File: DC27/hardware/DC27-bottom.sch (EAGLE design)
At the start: 2 parts

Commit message: removed inputs to output pins....duh
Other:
- note added: "Put a jumper between the FT2232HL and the rx/tx of the ESP. This will allow for using a usb to serial that isn't the FT2232HL otherwise the FT2232HL keeps the pins high"
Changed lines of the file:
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@@
 <drawing>
 <settings>
-<setting alwaysvectorfont="no"/>
+<setting alwaysvectorfont="yes"/>
 <setting verticaltext="up"/>
 </settings>
@@
 </instances>
 <busses>
+</busses>
+<nets>
+</nets>
+</sheet>
+<sheet>
+<plain>
+<text x="-10.16" y="81.28" size="1.778" layer="91">Put a jumper between the FT2232HL and the rx/tx of the ESP. This will allow for using a usb to serial that isn't the FT2232HL otherwise the FT2232HL keeps the pins high</text>
+</plain>
+<instances>
+</instances>
+<busses>

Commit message: moving over schema
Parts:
- removed U$2: CMD_C0DE_LOGO, darknet_parts_library:CMD_C0DE_LOGO
- added ATTINY13A: Header, connector:M06SILK_FEMALE_PTH
- added C1, C13, C22, C23, C24, C25: 10 uf, passives:C-USC0805
- added C10, C11, C12, C14, C15, C16, C17, C19, C21, C3, C32, C35, C8: 0.1 uF, passives:C-USC0805
- added C18, C2, C20: 4.7 uF, passives:C-USC0805
- added C26, C27, C28, C29: 15 pF, passives:C-USC0805
- added C33, C34: 10 uF, passives:C-USC0805
- added C4, C5: 1 uF, passives:C-USC0805
- added C6, C7: 27 pF, passives:C-USC0805
- added C9: 3.3 uF, passives:C-USC0805
- added D1: (no value), passives:DIODESMA
- added EMIFILTER1, EMIFILTER2: MEM2012S101RT, passives:MEM2012S101RT
- added ESP-PROG, ESP-RST: UserButton, dc-26:SWITCH_TACTILETACTILE-2PIN-NARROW
- added F1: ABLS-12.000MHZ-B4-T, crystals-timing:ABLS-12.000MHZ-B4-T
- added IC-IP5305: IP5305ESOP8, charging-ic:IP5305ESOP8
- added IC1: ATTINY13A-SSU, ICs:ATTINY13A-SSU
- added IC2: LDL112D33R, voltage-regulator:LDL112D33R
- added IC3: FT2232HL-REEL, ICs:FT2232HL-REEL
- added IC4: 93LC46BT-I_OT, eeprom:93LC46BT-I_OT
- added IC5, IC6, IC7, IC8: APA104, leds:APA104
- added J1: (no value), connector:M14
- added J3: (no value), connector:M02JST-PTH-2
- added J4: DN PAIR, connector:M04PTH
- added J8: (no value), connector:M06NO_SILK_YES_STOP
- added L1: 2.2uH, passives:NRS4018T2R2MDGJ
- added LED1, LED4, LED5, LED6, LED7, LED8: (no value), leds:LED3MM
- added LED2: rx-led, leds:LED3MM
- added LED3: tx-led, leds:LED3MM
- added OFF/ON: (no value), switches:SWITCH-SPSTPTH
- added R1, R4: 10K, dc-26:RESISTOR0805-RES
- added R10: 2.2K, passives:RESISTOR0805-RES
- added R11, R12: 56, passives:RESISTOR0805-RES
- added R13, R14: 100 R, passives:RESISTOR0805-RES
- added R15, R18, R19, R20: 100 R, dc-26:RESISTOR0805-RES
- added R16: 4.7 K, passives:RESISTOR0805-RES
- added R17, R22: 10 K, passives:RESISTOR0805-RES
- added R2: 10 R, passives:RESISTOR0805-RES
- added R21: 4K7, passives:RESISTOR0805-RES
- added R3: 20 R, passives:RESISTOR0805-RES
- added R5: 1K, passives:RESISTOR0805-RES
- added R6: 12 K, passives:RESISTOR0805-RES
- added R7, R8, R9: 10K, passives:RESISTOR0805-RES
- added RESETTABLE_FUSE: 0ZCJ0050FF2G, passives:0ZCJ0050FF2G
- added U$3: DX4R005JJ2DX4R005JJ2, connector:DX4R005JJ2DX4R005JJ2
- added U$4: ATECC608A-SSHDA, ICs:ATECC608A-SSHDA
- added U$5: SWITCH_TACTILETACTILE-2PIN-NARROW, switches:SWITCH_TACTILETACTILE-2PIN-NARROW
- added U$6: DC-27-SAO, defcon:DC-27-SAO
- added U$7: KRUX_LOGO, logos:KRUX_LOGO
- added U$8: CMD_C0DE_LOGO, logos:CMD_C0DE_LOGO
- added U$9: DN_LOGODC26, logos:DN_LOGODC26
- added U2: ESP-WROOM-32, ICs:ESP-WROOM-32
- U$1: value KRUX_LOGO -> M06X2; device darknet_parts_library:KRUX_LOGO -> connector:M06X2
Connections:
- new net ATTINY_ESP_CON: ATTINY13A.2, IC1.[PCINT3/CLKI/ADC3]_PB3, R19.1
- new net DISPLAY_BACKLIT: C34.1, J1.4, R18.2
- new net DISPLAY_CS: J1.5, U2.IO17
- new net DISPLAY_DATA_CMD: J1.3, U2.IO4
- new net DISPLAY_RESET: C2.1, J1.2, R15.2
- new net DISPLAY_SD_MISO: J1.8, U2.IO19
- new net DISPLAY_SD_MOSI: J1.13, U2.IO23
- new net DISPLAY_SD_SCK: J1.7, U2.IO18
- new net EECLK: IC3.EECLK, IC4.CLK, R8.2
- new net EECS: IC3.EECS, IC4.CS, R7.1
- new net EEDATA: IC3.EEDATA, IC4.DI, R10.2
- new net ESP-EN: ESP-RST.C, R4.1, U2.EN
- new net ESP-IO0: ESP-PROG.A, R1.1, U2.IO0
- new net ESP_ATTINY_CON: R19.2, U2.IO2
- new net ESP_LED1: R20.2, U2.IO16
- new net GND: C1.2, C10.2, C11.2, C12.2, C13.1, C14.2, C15.2, C16.2, C17.2, C18.2, C19.2, C2.2, C20.2, C21.2, C22.1, C23.1, C24.1, C25.2, C26.2, C27.2, C28.2, C29.2, C3.2, C32.2, C33.2, C34.2, C35.2, C4.2, C5.2, C6.2, C7.2, C8.2, C9.2, EMIFILTER1.GND_1, EMIFILTER1.GND_2, EMIFILTER2.GND_1, EMIFILTER2.GND_2, ESP-PROG.C, ESP-RST.A, IC-IP5305.9, IC1.GND, IC2.GND(1), IC2.GND(2), IC2.GND(3), IC2.GND(4), IC3.AGND, IC3.GND_1, IC3.GND_2, IC3.GND_3, IC3.GND_4, IC3.GND_5, IC3.GND_6, IC3.GND_7, IC3.GND_8, IC3.TEST, IC4.VSS, IC5.VSS, IC6.VSS, IC7.VSS, IC8.VSS, J1.14, J3.2, J8.3, LED7.C, LED8.C, OFF/ON.O, R22.1, R6.2, U$1.2, U$3.GND, U$4.GND, U$5.A, U$6.GND, U2.GND, U2.GND@1, U2.GND@15, U2.GND@38
- new net GPIO_APA104_DATA: ATTINY13A.1, IC1.[PCINT4/ADC2]_PB4, IC5.DIN
- new net JTAG_CLK: IC3.ADBUS0, U2.IO13
- new net JTAG_TDI: IC3.ADBUS1, U2.IO12
- new net JTAG_TDO: IC3.ADBUS2, U2.IO15
- new net JTAG_TMS: IC3.ADBUS3, U2.IO14
- new net N$1: D1.C, U$6.3V3
- new net N$10: C23.2, C24.2, IC-IP5305.8, RESETTABLE_FUSE.1
- new net N$11: LED2.A, R11.1
- new net N$12: IC6.DOUT, IC7.DIN
- new net N$13: LED3.A, R12.1
- new net N$14: IC-IP5305.3, LED5.A, LED6.C
- new net N$15: IC-IP5305.4, LED1.C, LED4.A, LED5.C, LED6.A
- new net N$16: C22.2, R2.2
- new net N$17: IC-IP5305.7, L1.2
- new net N$18: C18.1, C19.1, EMIFILTER2.OUT/IN, IC3.VPLL
- new net N$19: C20.1, C21.1, EMIFILTER1.OUT/IN, IC3.VPHY
- new net N$2: IC2.EN, OFF/ON.P
- new net N$20: C25.1, IC-IP5305.6, J3.1, L1.1
- new net N$21: IC-IP5305.5, R17.1, R3.1
- new net N$22: IC7.DOUT, IC8.DIN
- new net N$24: LED7.A, R3.2
- new net N$25: R17.2, U$5.C
- new net N$31: R14.1, U$1.9
- new net N$32: R13.1, U$1.7
- new net N$4: IC5.DOUT, IC6.DIN
- new net N$5: IC-IP5305.2, LED1.A, LED4.C
- new net N$6: IC3.RESET#, R5.2
- new net N$7: IC3.REF, R6.1
- new net N$8: IC4.DO, R10.1, R9.1
- new net N$9: LED8.A, R20.1
- new net OSCI: C6.1, F1.A, IC3.OSCI
- new net OSCO: C7.1, F1.K, IC3.OSCO
- new net PAIR_RX: J4.2, U2.IO34
- new net PAIR_TX: J4.1, U2.IO25
- new net PB0: ATTINY13A.6, IC1.PB0_[MOSI/AIN0/OC0A/PCINT0]
- new net PB1: ATTINY13A.5, IC1.PB1_[MISO/AIN1/OC0B/INT0/PCINT1]
- new net PB2: ATTINY13A.4, IC1.PB2_[SCK/ADC1/T0/PCINT2]
- new net PB5: ATTINY13A.3, IC1.PCINT5/!RESET!/ADC0/DW]_PB5, R16.1
- new net PROG_RX: R14.2, U2.RXD0
- new net PROG_TX: R13.2, U2.TXD0
- new net PWREN: IC3.PWREN#, U$1.1
- new net PWRSAV: IC3.BCBUS7, R21.2, R22.2
- new net RXD_LED: IC3.BCBUS3, LED2.C
- new net RXD_SPI_PROM_MOSI: IC3.BDBUS1, J1.11, U$1.8
- new net SAO-GPIO1: U$6.GPIO1
- new net SAO-GPIO2: U$6.GPIO2
- new net SCL: J1.12, U$4.SCL, U$6.SCL, U2.IO22
- new net SDA: J1.9, U$4.SDA, U$6.SDA, U2.IO21
- new net SD_CS: J1.6, U2.IO5
- new net SPI_PROM_CS: IC3.BDBUS3, U$1.4
- new net SPI_PROM_MISO: IC3.BDBUS2, U$1.6
- new net SUSPEND: IC3.SUSPEND__#, U$1.3
- new net SVN: J4.3, U2.SENSOR_VN
- new net SVP: J4.4, U2.SENSOR_VP
- new net TOUCH_CLK: J8.2, U2.IO26
- new net TOUCH_CS: J8.1, U2.IO27
- new net TOUCH_DATA_IN: J8.6, U2.IO35
- new net TOUCH_DATA_OUT: J8.4, U2.IO33
- new net TOUCH_IRQ: J8.5, U2.IO32
- new net TXD_LED: IC3.BCBUS4, LED3.C
- new net TXD_SPI_PROM_CLK: IC3.BDBUS0, J1.10, U$1.10
- new net USB_DM: IC3.DM, U$3.D-
- new net USB_DP: IC3.DP, U$3.D+
- new net VBAT: C26.1, C27.1, C28.1, C29.1, C32.1, C33.1, C4.1, IC1.VCC, IC2.VIN, IC5.VDD, IC6.VDD, IC7.VDD, IC8.VDD, OFF/ON.S, R16.2, RESETTABLE_FUSE.2
- new net VCC: C1.1, C11.1, C14.1, C15.1, C16.1, C3.1, C35.1, C5.1, C8.1, D1.A, EMIFILTER1.IN/OUT, EMIFILTER2.IN/OUT, IC2.VOUT, IC3.VCCIO_1, IC3.VCCIO_2, IC3.VCCIO_3, IC3.VCCIO_4, IC3.VREGIN, IC4.VCC, J1.1, R1.2, R11.2, R12.2, R15.1, R18.1, R4.2, R5.1, R7.2, R8.1, R9.2, U$1.12, U$4.VCC, U2.3V3
- new net VCC1.8: C10.1, C12.1, C17.1, C9.1, IC3.VCORE_1, IC3.VCORE_2, IC3.VCORE_3, IC3.VREGOUT
- new net VCC5V: C13.2, IC-IP5305.1, R2.1, R21.1, U$3.+5V
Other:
- note added: "If we don't connect RESX line to a GPIO (and I'm not to save GPIO pins), we need to ensure RESX stay low for 10 us. So I'm going to set it up to stay low via a capacitor for 470 us by using a 4.7 uF cap and a 100 Ohm resistor calculator used: https://www.allaboutcircuits.com/tools/capacitor-Charge-and-time-constant-calculator/ same for back light, except using a larger cap to delay even longer"
- note added: "Pins 60, 36, and 59 need to be revisited to allow for external control of suspend."
- note added: "output pins: pwren: low = normal, high USB suspend suspend: low when in USB suspend"
- note added: "vcc5v is from USB. If usb plugged in pwrsav goes high and ft2232HL turns on, if unplugged it turns off."

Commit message: dc27 board started for darknet 8
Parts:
- removed ATTINY13A: Header, connector:M06SILK_FEMALE_PTH
- removed C32: 0.1 uF, passives:C-USC0805
- removed C33: 10 uF, passives:C-USC0805
- removed F1: ABLS-12.000MHZ-B4-T, crystals-timing:ABLS-12.000MHZ-B4-T
- removed IC1: ATTINY13A-SSU, ICs:ATTINY13A-SSU
- removed IC5, IC6, IC7, IC8: APA104, leds:APA104
- removed J4: DN PAIR, connector:M04PTH
- removed J8: (no value), connector:M06NO_SILK_YES_STOP
- removed R19, R20: 100 R, dc-26:RESISTOR0805-RES
- removed R21: 4K7, passives:RESISTOR0805-RES
- added J2: JTAG, connector:M04X2
- added R23, R24, R25, R26: 100 R, dc-26:RESISTOR0805-RES
- added U$10: 2.4-SPI-TFT-TOUCH-SSD-MODULE, displays:2.4-SPI-TFT-TOUCH-SSD-MODULE
- added U$11, U$12, U$13, U$14: APA1025050, leds:APA1025050
- added U$2: XBP15SRV05W-G, passives:XBP15SRV05W-G
- added Y1: ABM7-12.000MHZ-D2Y-T, crystals-timing:ABM7-12.000MHZ-D2Y-T
- C1, C13, C22, C23, C24, C25: value 10 uf -> 10 uF
- C6, C7: value 27 pF -> 18 pF
- D1: value (none) -> SAO-Diode
- J1: value (none) -> DN PAIR; device connector:M14 -> connector:M03X22X3_SILK_MALE_PTH
- J3: value (none) -> Battery
- LED1: value (none) -> cl1
- LED4: value (none) -> cl2
- LED5: value (none) -> cl3
- LED6: value (none) -> cl4
- LED7: value (none) -> KeyLed
- LED8: value (none) -> ESP-LED
- OFF/ON: value (none) -> Brd Power; device switches:SWITCH-SPSTPTH -> switches:SWITCH-SPSTKIT
- R1, R4, R7, R8, R9: value 10K -> 10 K
- R10: value 2.2K -> 2.2 K
- R11, R12: value 56 -> 56 R
- R3: value 20 R -> 10 R
- R5: value 1K -> 1 K
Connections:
- removed net ATTINY_ESP_CON: ATTINY13A.2, IC1.[PCINT3/CLKI/ADC3]_PB3, R19.1
- removed net ESP_ATTINY_CON: R19.2, U2.IO2
- removed net ESP_LED1: R20.2, U2.IO16
- removed net GPIO_APA104_DATA: ATTINY13A.1, IC1.[PCINT4/ADC2]_PB4, IC5.DIN
- removed net JTAG_TDO: IC3.ADBUS2, U2.IO15
- removed net N$12: IC6.DOUT, IC7.DIN
- removed net N$22: IC7.DOUT, IC8.DIN
- removed net N$4: IC5.DOUT, IC6.DIN
- removed net N$9: LED8.A, R20.1
- removed net PB0: ATTINY13A.6, IC1.PB0_[MOSI/AIN0/OC0A/PCINT0]
- removed net PB1: ATTINY13A.5, IC1.PB1_[MISO/AIN1/OC0B/INT0/PCINT1]
- removed net PB2: ATTINY13A.4, IC1.PB2_[SCK/ADC1/T0/PCINT2]
- removed net PB5: ATTINY13A.3, IC1.PCINT5/!RESET!/ADC0/DW]_PB5, R16.1
- new net APA102_CLK: U$13.CI, U2.IO2
- new net APA102_DATA: U$13.DI, U2.IO16
- new net ESP_JTAG_CLK: J2.8, R23.1
- new net ESP_JTAG_TDI: J2.6, R25.1
- new net ESP_JTAG_TDO_LED: J2.4, LED8.A, R24.1
- new net ESP_JTAG_TMS: J2.2, R26.1
- new net FT_JTAG_CLK: IC3.ADBUS0, J2.7
- new net FT_JTAG_TDI: IC3.ADBUS1, J2.5
- new net FT_JTAG_TDO: IC3.ADBUS2, J2.3
- new net FT_JTAG_TMS: IC3.ADBUS3, J2.1
- new net JTAG_TDO_LED1: R24.2, U2.IO15
- new net N$28: U$11.GND, U$12.GND, U$13.GND, U$14.GND
- new net N$34: U$11.CI, U$12.CO
- new net N$35: U$11.DI, U$12.DO
- new net N$36: U$12.CI, U$14.CO
- new net N$37: U$12.DI, U$14.DO
- new net N$38: U$13.DO, U$14.DI
- new net N$39: U$13.CO, U$14.CI
- net DISPLAY_BACKLIT: now also U$10.LED; no longer J1.4
- net DISPLAY_CS: now also U$10.CS; no longer J1.5
- net DISPLAY_DATA_CMD: now also U$10.D/C; no longer J1.3
- net DISPLAY_RESET: now also U$10.RESET; no longer J1.2
- net DISPLAY_SD_MISO: now also U$10.MISO, U$10.SD_MISO; no longer J1.8
- net DISPLAY_SD_MOSI: now also U$10.MOSI, U$10.SD_MOSI; no longer J1.13
- net DISPLAY_SD_SCK: now also U$10.SCK, U$10.SD_SCK; no longer J1.7
- net ESP-IO0: now also ESP-PROG.C; no longer ESP-PROG.A
- net GND: now also ESP-PROG.A, U$10.GND, U$2.P2; no longer C32.2, C33.2, ESP-PROG.C, IC1.GND, IC5.VSS, IC6.VSS, IC7.VSS, IC8.VSS, J1.14, J8.3
- net JTAG_CLK: now also R23.2; no longer IC3.ADBUS0
- net JTAG_TDI: now also R25.2; no longer IC3.ADBUS1
- net JTAG_TMS: now also R26.2; no longer IC3.ADBUS3
- net OSCI: now also Y1.2; no longer F1.A
- net OSCO: now also Y1.1; no longer F1.K
- net PAIR_RX: now also J1.3; no longer J4.2
- net PAIR_TX: now also J1.5; no longer J4.1
- net PWRSAV: now also R16.2; no longer R21.2
- net RXD_SPI_PROM_MOSI: no longer J1.11
- net SAO-GPIO1: now also J1.4
- net SAO-GPIO2: now also J1.6
- net SCL: no longer J1.12
- net SDA: no longer J1.9
- net SD_CS: now also U$10.SD_CS; no longer J1.6
- net SVN: now also J1.1; no longer J4.3
- net SVP: now also J1.2; no longer J4.4
- net TOUCH_CLK: now also U$10.T_CLK; no longer J8.2
- net TOUCH_CS: now also U$10.T_CS; no longer J8.1
- net TOUCH_DATA_IN: now also U$10.T_DIN; no longer J8.6
- net TOUCH_DATA_OUT: now also U$10.T_DO; no longer J8.4
- net TOUCH_IRQ: now also U$10.T_IRQ; no longer J8.5
- net TXD_SPI_PROM_CLK: no longer J1.10
- net USB_DM: now also U$2.P1
- net USB_DP: now also U$2.P6
- net VBAT: no longer C26.1, C27.1, C28.1, C29.1, C32.1, C33.1, IC1.VCC, IC5.VDD, IC6.VDD, IC7.VDD, IC8.VDD, R16.2
- net VCC: now also C26.1, C27.1, C28.1, C29.1, U$10.VCC, U$11.VCC, U$12.VCC, U$13.VCC, U$14.VCC; no longer J1.1
- net VCC5V: now also R16.1; no longer R21.1
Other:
- note added: "dn pair: can jumper pair pins to sao gpio pins"
- note removed: "Pins 60, 36, and 59 need to be revisited to allow for external control of suspend."
- note removed: "Put a jumper between the FT2232HL and the rx/tx of the ESP. This will allow for using a usb to serial that isn't the FT2232HL otherwise the FT2232HL keeps the pins high"

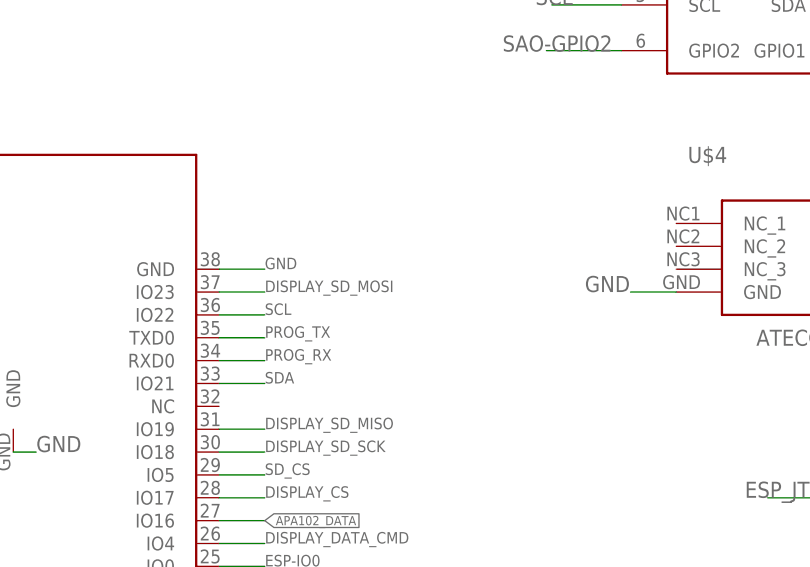
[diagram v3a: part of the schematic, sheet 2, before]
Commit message: started on changes to not charlie plex the leds
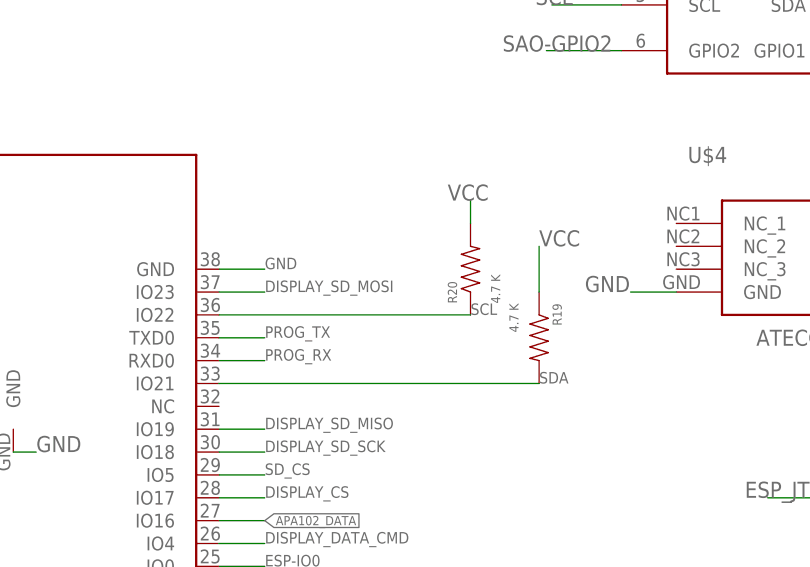
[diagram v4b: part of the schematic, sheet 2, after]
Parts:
- added R19, R20: 4.7 K, dc-26:RESISTOR0805-RES
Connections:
- net SCL: now also R20.1
- net SDA: now also R19.2
- net VCC: now also R19.1, R20.2

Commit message: basic layout nearly done
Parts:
- removed C26, C27, C28, C29: 15 pF, passives:C-USC0805
- removed D1: SAO-Diode, passives:DIODESMA
- removed U$11, U$12, U$13, U$14: APA1025050, leds:APA1025050
- removed U$6: DC-27-SAO, defcon:DC-27-SAO
- added TOP-BOT-CONNECTOR: M06X2, connector:M06X2
- LED1, LED2, LED3, LED4, LED5, LED6, LED7, LED8: device leds:LED3MM -> leds:LED1206
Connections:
- removed net N$1: D1.C, U$6.3V3
- removed net N$28: U$11.GND, U$12.GND, U$13.GND, U$14.GND
- removed net N$34: U$11.CI, U$12.CO
- removed net N$35: U$11.DI, U$12.DO
- removed net N$36: U$12.CI, U$14.CO
- removed net N$37: U$12.DI, U$14.DO
- removed net N$38: U$13.DO, U$14.DI
- removed net N$39: U$13.CO, U$14.CI
- net APA102_CLK: now also TOP-BOT-CONNECTOR.5; no longer U$13.CI
- net APA102_DATA: now also TOP-BOT-CONNECTOR.3; no longer U$13.DI
- net GND: now also J3.1, TOP-BOT-CONNECTOR.11, TOP-BOT-CONNECTOR.12; no longer C26.2, C27.2, C28.2, C29.2, J3.2, U$6.GND
- net N$20: now also J3.2; no longer J3.1
- net SAO-GPIO1: now also TOP-BOT-CONNECTOR.8; no longer U$6.GPIO1
- net SAO-GPIO2: now also TOP-BOT-CONNECTOR.10; no longer U$6.GPIO2
- net SCL: now also TOP-BOT-CONNECTOR.4; no longer U$6.SCL
- net SDA: now also TOP-BOT-CONNECTOR.6; no longer U$6.SDA
- net VBAT: now also TOP-BOT-CONNECTOR.1
- net VCC: now also TOP-BOT-CONNECTOR.2; no longer C26.1, C27.1, C28.1, C29.1, D1.A, U$11.VCC, U$12.VCC, U$13.VCC, U$14.VCC

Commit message: what should be sent to pcbway
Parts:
- U$7: value KRUX_LOGO -> KRUX_LOGOKRUX_LOGO_SILK; device logos:KRUX_LOGO -> logos:KRUX_LOGOKRUX_LOGO_SILK
- U$9: value DN_LOGODC26 -> DN_LOGO; device logos:DN_LOGODC26 -> logos:DN_LOGO
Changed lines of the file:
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@@
 <part name="R13" library="passives" deviceset="RESISTOR" device="0805-RES" value="100 R"/>
 <part name="R14" library="passives" deviceset="RESISTOR" device="0805-RES" value="100 R"/>
-<part name="U$7" library="logos" deviceset="KRUX_LOGO" device=""/>
-<part name="U$8" library="logos" deviceset="CMD_C0DE_LOGO" device=""/>
-<part name="U$9" library="logos" deviceset="DN_LOGO" device="DC26"/>
+<part name="U$7" library="logos" deviceset="KRUX_LOGO" device="KRUX_LOGO_SILK" value="KRUX_LOGOKRUX_LOGO_SILK"/>
+<part name="U$8" library="logos" deviceset="CMD_C0DE_LOGO" device="" value="CMD_C0DE_LOGO"/>
+<part name="U$9" library="logos" deviceset="DN_LOGO" device="" value="DN_LOGO"/>
 <part name="U$1" library="connector" deviceset="M06X2" device=""/>
 <part name="R22" library="passives" deviceset="RESISTOR" device="0805-RES" value="10 K"/>
